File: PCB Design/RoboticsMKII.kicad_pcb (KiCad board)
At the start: 4 copper layers, 89 parts, among them CON1 USB, CON2 BARREL_JACK, P1 Power Sel, P10 Camera, P11 DAC, P12 Reed, P13 SPI, P14 ICSP, P15 Gnd, P16 UART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

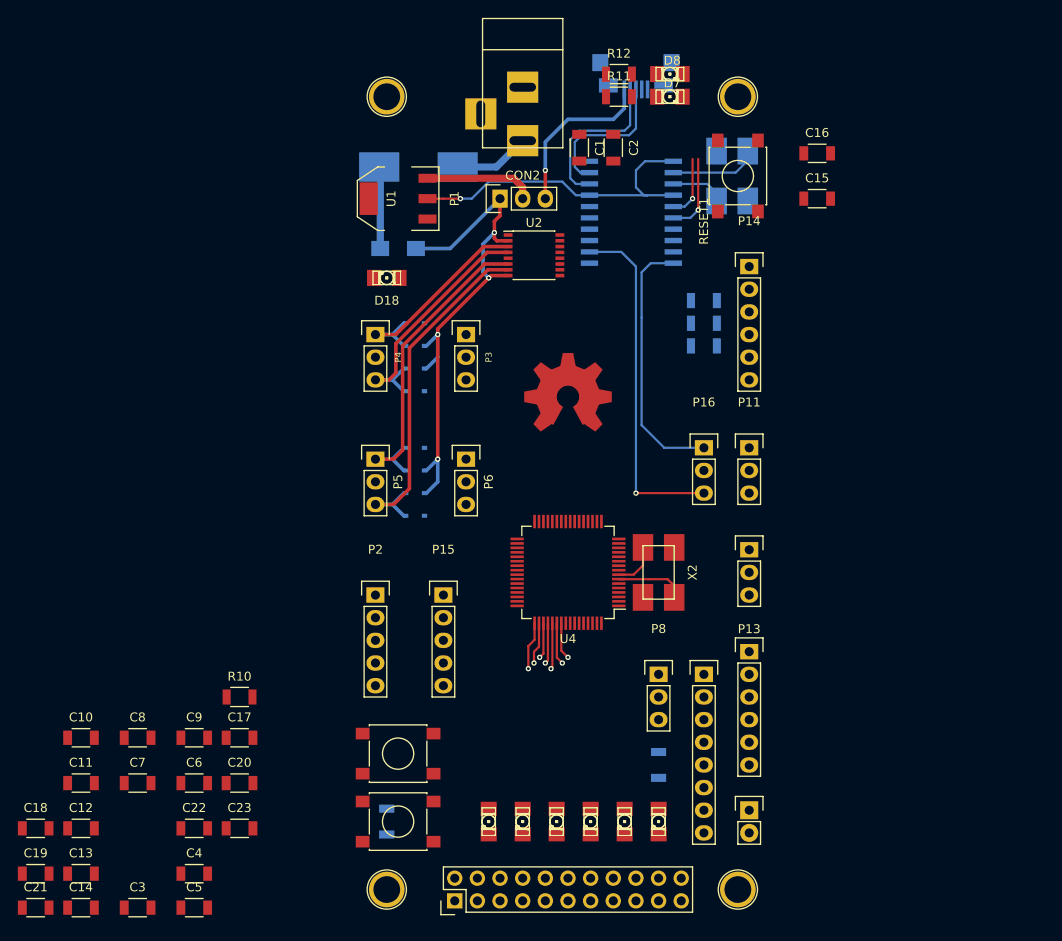
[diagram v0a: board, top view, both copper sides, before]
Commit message: More power layout, improved feedback diodes. All fonts now the same
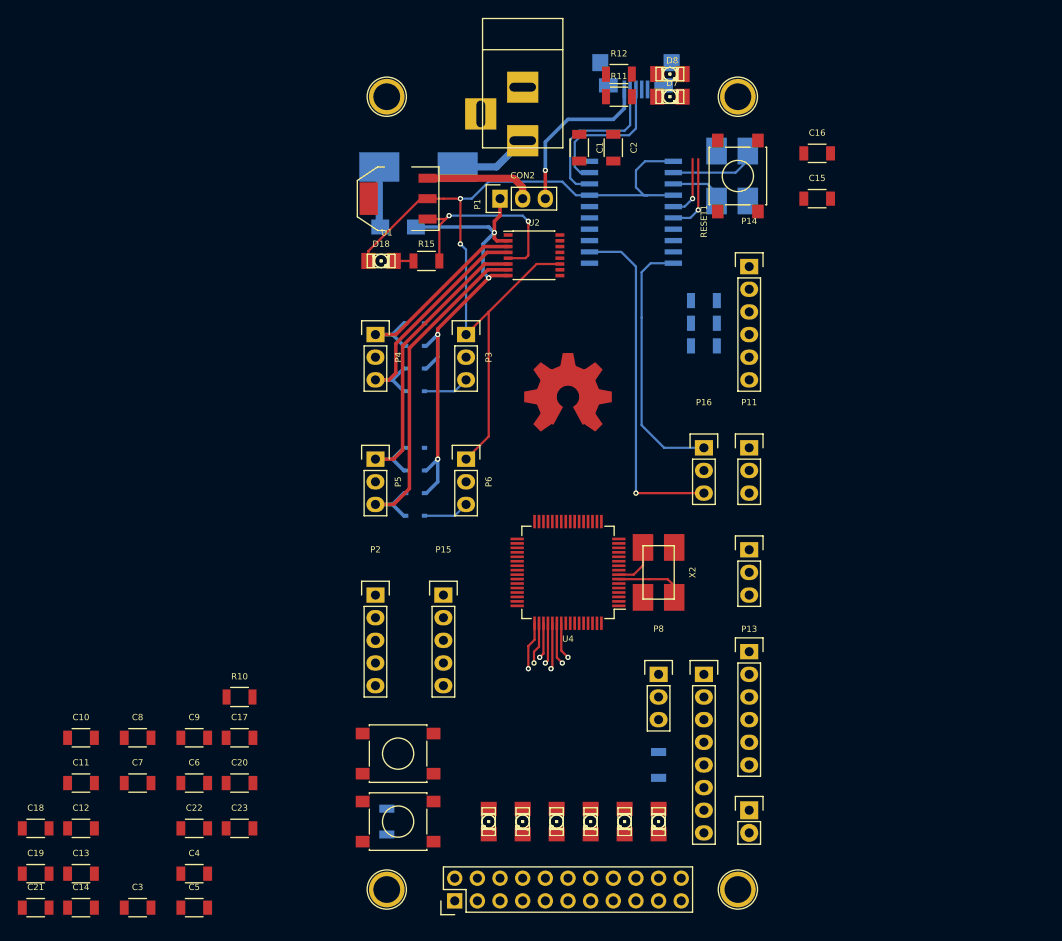
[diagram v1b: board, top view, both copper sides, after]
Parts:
- R15: moved to F.Cu
- moved R15 4.84 mm to (121.3, 65.4)
- moved F1 2.41 mm to (118.1, 61.6)
- moved D18 2.01 mm to (116.2, 65.4), turned to 0 degrees
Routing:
- net V3.3: track 37.1 -> 94.2 mm, vias 1 -> 2
- net GND: track 0.00 -> 33.8 mm, vias 0 -> 2
- net /motors/V_Bat: track 62.8 -> 60.2 mm
- net Net-(D9-Pad2): track 9.19 -> 6.94 mm
- net Net-(D18-Pad2): track 0.00 -> 2.21 mm

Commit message: Bus routing done. No idea what to do with the MCU oscillator.
Signed-off-by: Kolijn_Laptop <kolijn.wolfaardt@gmail.com>
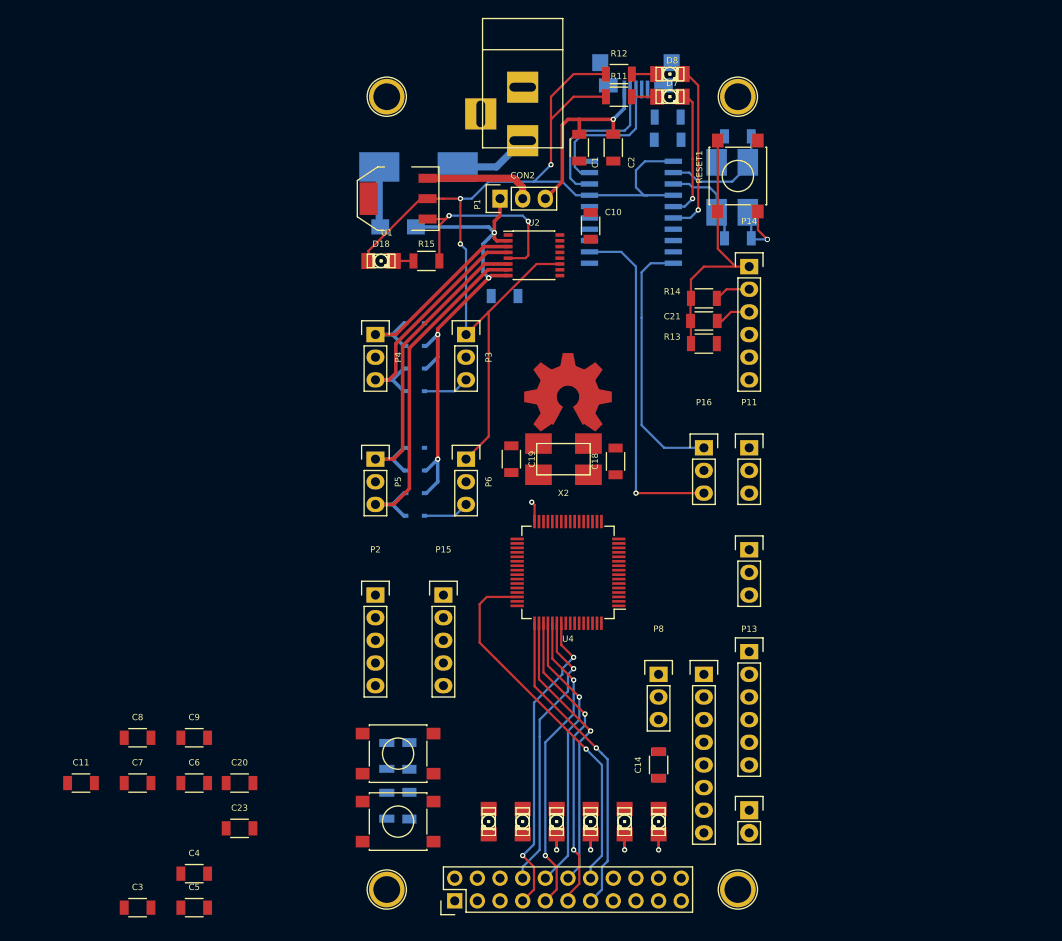
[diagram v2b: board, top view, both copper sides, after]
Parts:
- C12, C13, C15, C16, C17, C22, R10: moved to B.Cu
- R13, R14: moved to F.Cu
- moved C21 99.7 mm to (152.4, 72.1)
- moved C17 82.5 mm to (148.3, 51.8)
- moved C10 81.0 mm to (139.7, 61.5), turned to 270 degrees
- moved R10 80.8 mm to (148.3, 49.3)
- moved C18 76.9 mm to (142.5, 87.9), turned to 90 degrees
- moved C19 70.8 mm to (130.8, 87.6), turned to 270 degrees
- moved C22 69.1 mm to (130.0, 69.3)
- moved C14 66.7 mm to (147.3, 121.9), turned to 90 degrees
- moved R2 58.1 mm to (116.8, 120.9), turned to 90 degrees
- moved C12 37.7 mm to (119.4, 120.9), turned to 270 degrees
- moved C13 37.6 mm to (119.4, 126.5), turned to 270 degrees
- moved X2 16.6 mm to (136.7, 87.6), turned to 0 degrees
- moved C16 13.0 mm to (156.2, 62.9)
- moved C15 11.3 mm to (156.2, 51.4), turned to 180 degrees
- moved R13 2.29 mm to (152.4, 74.7)
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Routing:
- net /gpio/DATA_0: track 0.00 -> 41.5 mm, vias 0 -> 1
- net /gpio/DATA_7: track 4.14 -> 35.1 mm, vias 1 -> 2
- net /gpio/DATA_3: track 4.00 -> 34.4 mm, vias 1 -> 2
- net /gpio/DATA_1: track 5.38 -> 35.3 mm
- net /gpio/DATA_5: track 5.16 -> 34.5 mm, vias 1 -> 2
- net /mcu/MCLR_in: track 0.00 -> 29.3 mm
- net V3.3: track 94.2 -> 123.0 mm, vias 2 -> 3
- net /gpio/DATA_2: track 4.69 -> 32.0 mm
- net /gpio/DATA_4: track 4.58 -> 31.6 mm
- net /gpio/DATA_6: track 4.71 -> 31.7 mm
- net GND: track 33.8 -> 46.3 mm, vias 2 -> 3
- net /usb/RX_LED: track 8.88 -> 19.4 mm
- net /usb/TX_LED: track 6.97 -> 14.7 mm
- net /usb/USB_OSC2: track 6.15 -> 10.6 mm
- net /mcu/OSC2: track 4.37 -> 0.00 mm
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
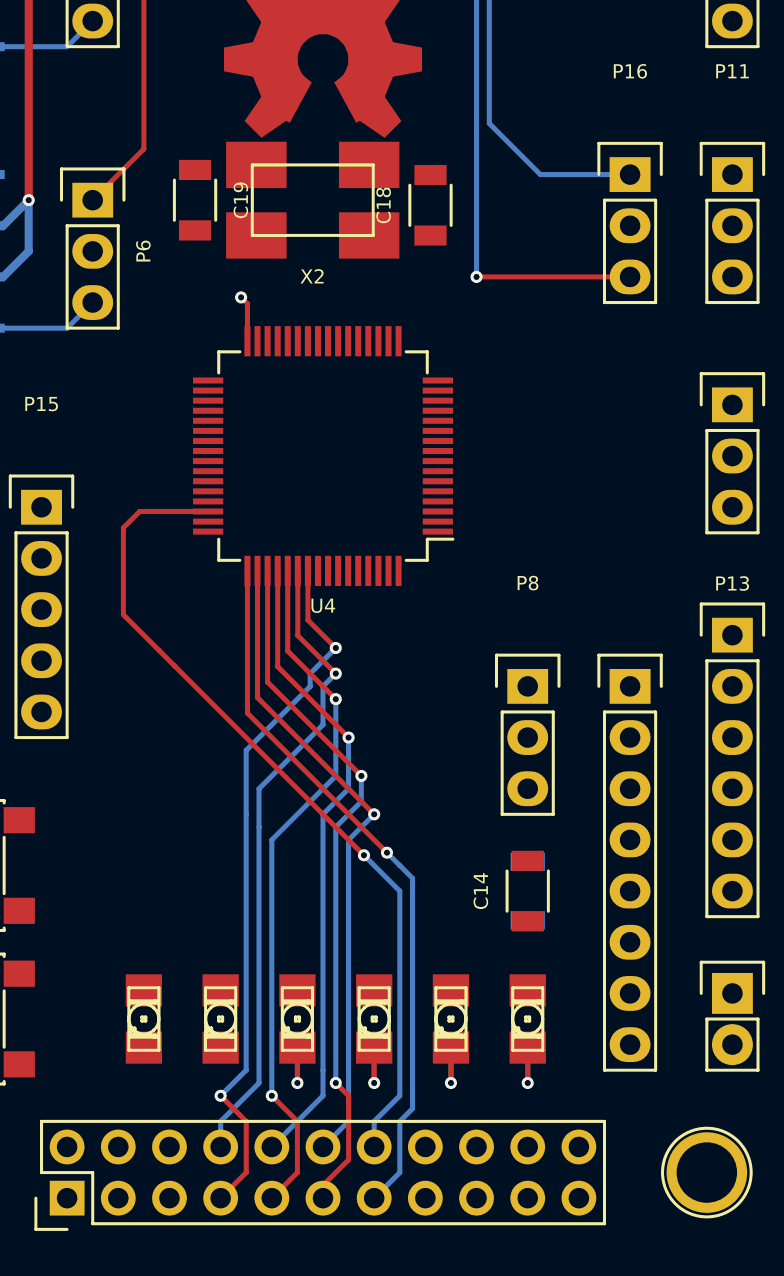
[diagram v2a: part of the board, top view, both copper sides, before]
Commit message: Removed bus, rotated mcu to fit crystal in
Signed-off-by: Kolijn_Laptop <kolijn.wolfaardt@gmail.com>
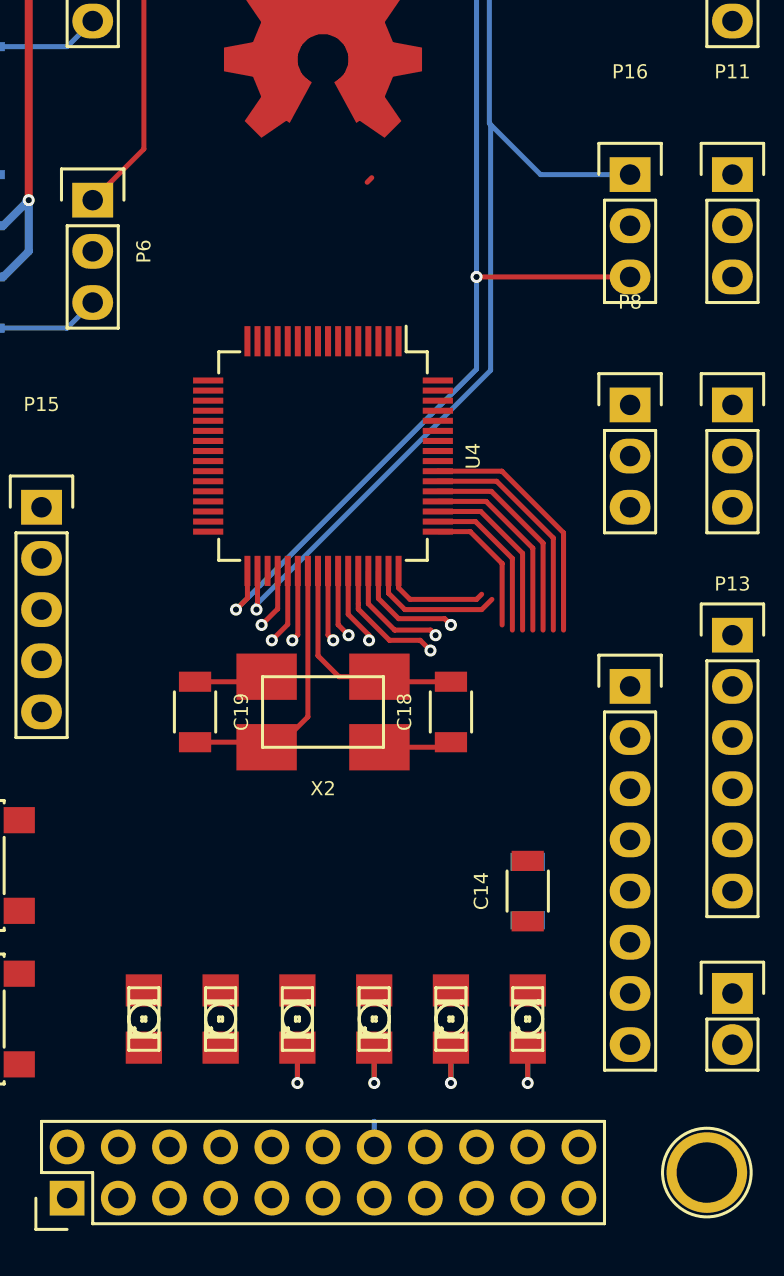
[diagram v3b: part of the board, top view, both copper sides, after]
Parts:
- moved X2 25.4 mm to (137.2, 113.0)
- moved C19 25.4 mm to (130.8, 113.0)
- moved C18 25.2 mm to (143.5, 113.0)
- moved P8 14.9 mm to (152.4, 97.8)
- turned U4 to 270 degrees
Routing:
- net /gpio/DATA_0: track 41.5 -> 6.83 mm
- net /usb/MCU_RX: track 29.2 -> 60.0 mm, vias 0 -> 1
- net /gpio/DATA_1: track 35.3 -> 7.48 mm, vias 1 -> 0
- net /gpio/DATA_3: track 34.4 -> 9.51 mm, vias 2 -> 0
- net /gpio/DATA_2: track 32.0 -> 8.01 mm, vias 1 -> 0
- net /gpio/DATA_5: track 34.5 -> 10.6 mm, vias 2 -> 0
- net /usb/MCU_TX: track 38.9 -> 62.5 mm, vias 1 -> 2
- net /gpio/DATA_7: track 35.1 -> 12.3 mm, vias 2 -> 0
- net /gpio/DATA_4: track 31.6 -> 9.74 mm, vias 1 -> 0
- net /gpio/DATA_6: track 31.7 -> 11.5 mm, vias 1 -> 0
- net /mcu/OSC2: track 0.00 -> 13.6 mm
- net /mcu/OSC1: track 0.32 -> 11.3 mm
- net GND: track 46.3 -> 57.2 mm, vias 3 -> 4
- net /mcu/PGD: track 0.00 -> 6.79 mm
- net /gpio/BUT_1: track 0.00 -> 6.33 mm, vias 0 -> 1
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
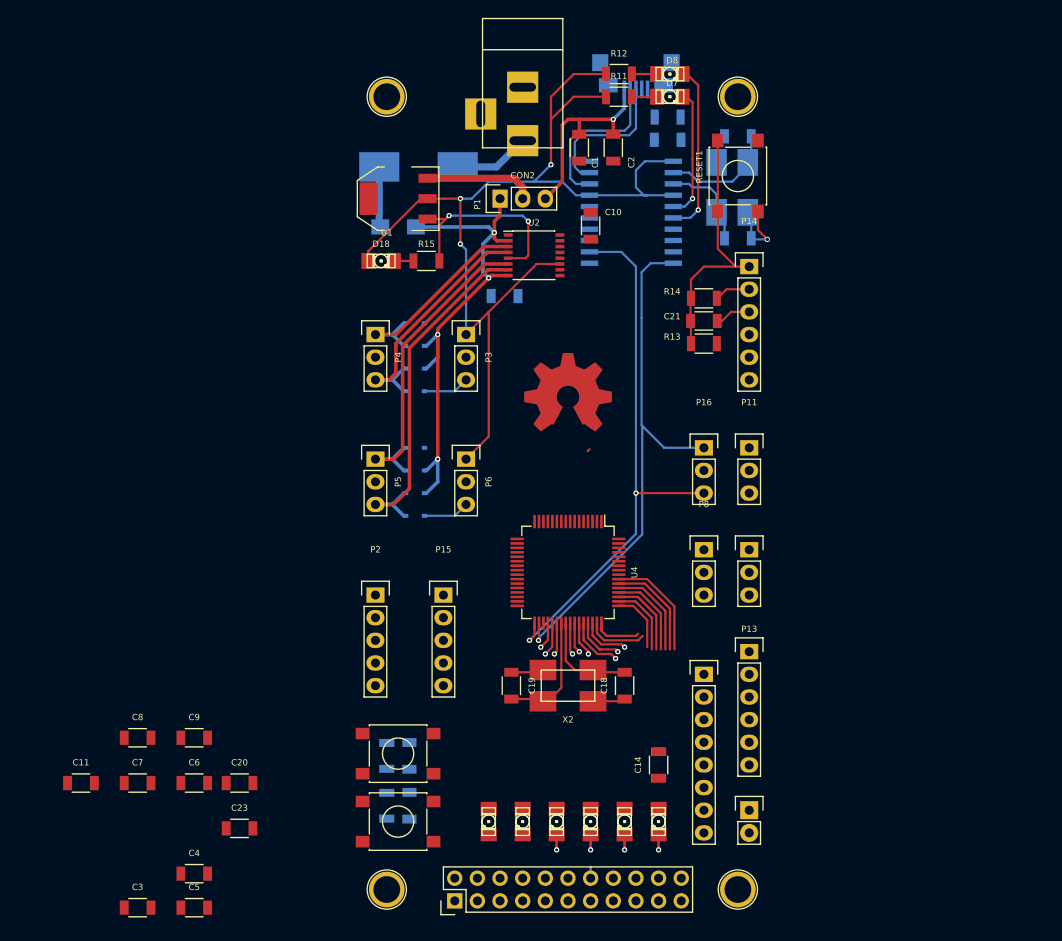
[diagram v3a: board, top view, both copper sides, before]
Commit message: Most of the Camera bus routed, analog bus routed as well. ICSP and SPI are next
Signed-off-by: Kolijn Wolfaardt <kolijn.wolfaardt@gmail.com>
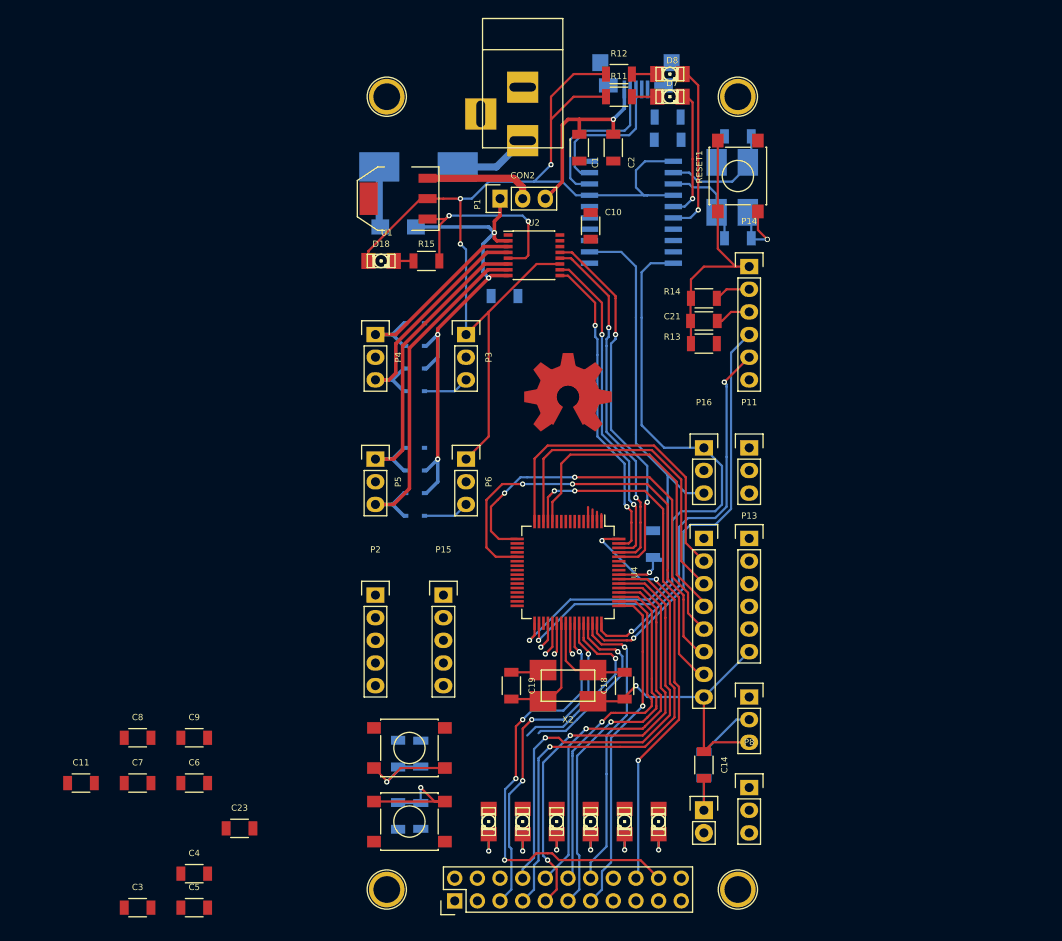
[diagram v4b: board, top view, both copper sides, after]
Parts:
- C20: moved to B.Cu
- moved C20 53.5 mm to (146.7, 97.2), turned to 270 degrees
- moved P8 27.1 mm to (157.5, 124.5)
- moved P7 16.5 mm to (157.5, 114.3)
- moved P9 15.2 mm to (152.4, 96.5)
- moved P13 12.7 mm to (157.5, 96.5)
- moved SW1 8.35 mm to (119.4, 120.0)
- moved R2 7.73 mm to (120.7, 127.6)
- moved SW0 7.73 mm to (119.4, 128.3)
- moved R7 6.97 mm to (120.7, 120.7)
- moved C12 6.85 mm to (118.1, 127.6), turned to 90 degrees
- moved C13 5.98 mm to (118.1, 120.7)
- moved C14 5.08 mm to (152.4, 121.9), turned to 270 degrees
- moved R9 5.08 mm to (152.4, 121.9)
- moved P12 5.08 mm to (152.4, 127.0)
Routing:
- net /gpio/AN4: track 0.00 -> 49.7 mm, vias 0 -> 2
- net /gpio/~OE: track 3.41 -> 51.3 mm, vias 1 -> 4
- net /gpio/RCK: track 0.00 -> 46.4 mm, vias 0 -> 3
- net /gpio/AN3: track 0.00 -> 44.7 mm, vias 0 -> 2
- net /mcu/MOT1_D1: track 0.00 -> 42.0 mm, vias 0 -> 2
- net /gpio/DATA_7: track 12.3 -> 53.8 mm, vias 0 -> 1
- net /mcu/PGD: track 6.79 -> 46.7 mm, vias 0 -> 1
- net /gpio/DATA_5: track 10.6 -> 50.4 mm, vias 0 -> 2
- net /mcu/MOT1_D2: track 0.00 -> 39.8 mm, vias 0 -> 2
- net /gpio/DATA_6: track 11.5 -> 51.1 mm, vias 0 -> 1
- net /mcu/PGC: track 5.31 -> 43.0 mm, vias 0 -> 2
- net /gpio/AN5: track 0.00 -> 37.5 mm, vias 0 -> 2
- net /mcu/MOT2_D1: track 0.00 -> 37.1 mm, vias 0 -> 2
- net /gpio/AN1: track 0.00 -> 37.0 mm
- net /gpio/AN2: track 0.00 -> 36.8 mm
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
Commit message: Most signals are done now, only power remains. This will definitely be a 4 layer board
Signed-off-by: Kolijn Wolfaardt <kolijn.wolfaardt@gmail.com>
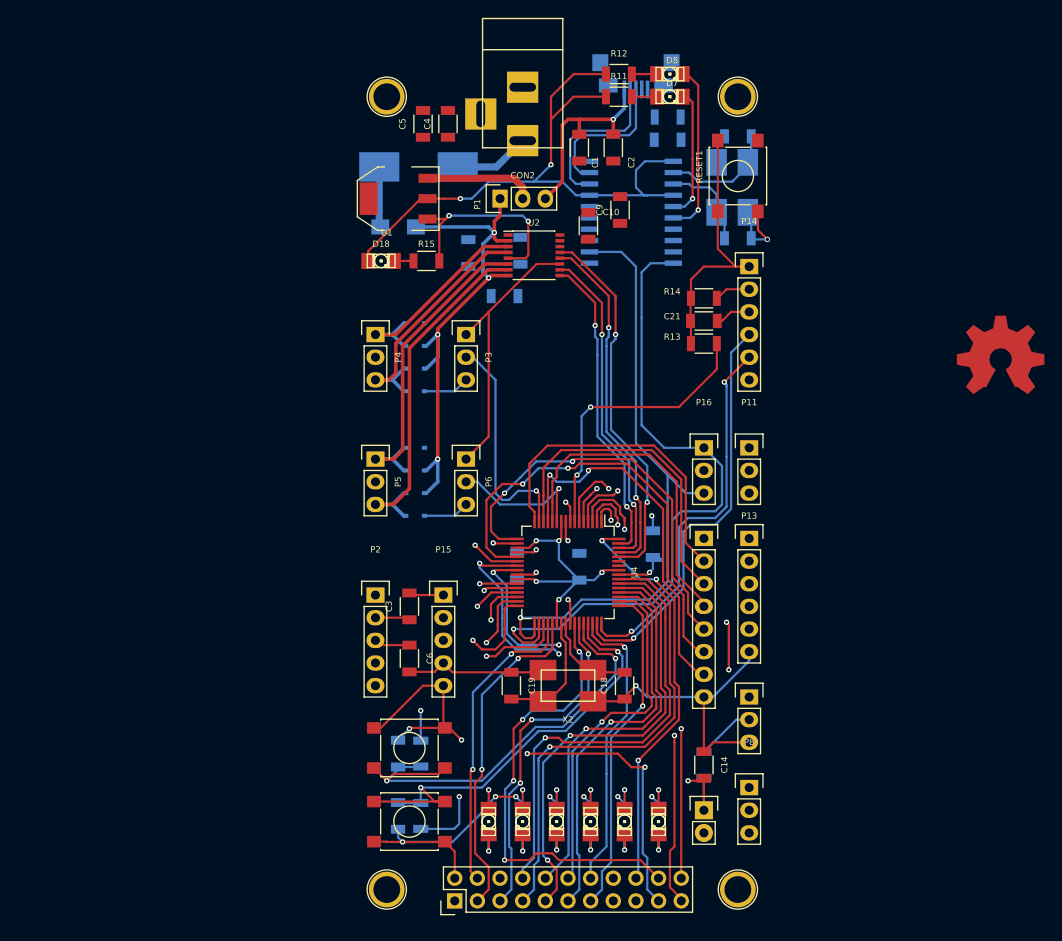
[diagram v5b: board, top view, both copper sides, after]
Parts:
- C11, C23, C7, C8: moved to B.Cu
- moved C5 91.6 mm to (120.9, 50.0), turned to 90 degrees
- moved C4 88.8 mm to (123.7, 50.0), turned to 90 degrees
- moved C9 76.0 mm to (143.0, 59.7), turned to 90 degrees
- moved C11 73.6 mm to (126.0, 64.5), turned to 270 degrees
- moved C23 72.0 mm to (131.8, 64.3), turned to 270 degrees
- moved C8 53.1 mm to (138.4, 99.7), turned to 90 degrees
- moved C7 49.0 mm to (131.4, 99.7), turned to 90 degrees
- moved OSHW_COPPER_10MM 48.7 mm to (185.7, 76.5)
- moved C3 45.5 mm to (119.4, 104.1), turned to 90 degrees
- moved C6 27.9 mm to (119.4, 110.0), turned to 270 degrees
- moved C10 0.25 mm to (139.4, 61.5)
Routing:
- net V3.3: track 133.1 -> 329.7 mm, vias 4 -> 9
- net GND: track 86.2 -> 195.7 mm, vias 5 -> 18
- net /gpio/~WRST: track 0.00 -> 58.6 mm, vias 0 -> 3
- net /gpio/~WR: track 0.00 -> 56.4 mm, vias 0 -> 3
- net /gpio/~RRST: track 0.00 -> 52.7 mm, vias 0 -> 3
- net /gpio/Href: track 0.00 -> 52.6 mm, vias 0 -> 1
- net /motors/PWM2: track 1.37 -> 47.3 mm, vias 0 -> 3
- net /gpio/LED0: track 0.00 -> 41.6 mm, vias 0 -> 2
- net /gpio/Reed: track 7.21 -> 48.8 mm, vias 0 -> 2
- net /gpio/LED1: track 0.00 -> 39.9 mm, vias 0 -> 2
- net /gpio/DACOUT: track 0.00 -> 39.7 mm, vias 0 -> 1
- net /gpio/LED5: track 0.00 -> 36.0 mm, vias 0 -> 2
- net /gpio/SIO_C: track 3.77 -> 37.5 mm, vias 1 -> 2
- net /motors/PWM1: track 0.84 -> 33.5 mm, vias 0 -> 1
- net /mcu/MCLR: track 0.00 -> 32.4 mm, vias 0 -> 2
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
